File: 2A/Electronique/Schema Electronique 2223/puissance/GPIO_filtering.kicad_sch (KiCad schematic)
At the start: 4 parts, among them J201 Conn_01x02

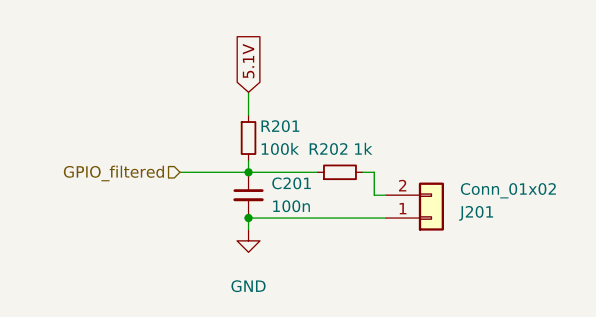
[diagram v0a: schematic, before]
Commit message: suppression diode et changement des feuille hiérarchique
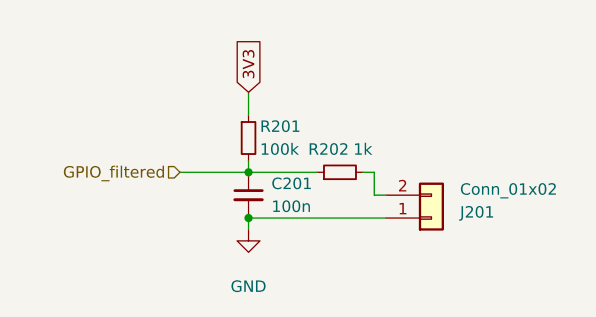
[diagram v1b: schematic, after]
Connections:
- net 5.1V renamed 3V3
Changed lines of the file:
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@@
     (stroke (width 0) (type default))
   )
-  (global_label "5.1V" (shape input) (at 124.46 73.66 90) (fields_autoplaced)
+  (global_label "3V3" (shape input) (at 124.46 73.66 90) (fields_autoplaced)
     (effects (font (size 1.27 1.27)) (justify left))
-    (property "Intersheetrefs" "${INTERSHEET_REFS}" (at 124.46 66.5624 90)
+    (property "Intersheetrefs" "${INTERSHEET_REFS}" (at 124.46 67.1672 90)
       (effects (font (size 1.27 1.27)) (justify left) hide)
     )

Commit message: update puissance
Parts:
- removed C201: 100n, Capacitor_SMD:C_0402_1005Metric, symbol Device:C_Small
- removed J201: Conn_01x02, symbol Connector_Generic:Conn_01x02
- removed R201: 100k, Resistor_SMD:R_0402_1005Metric, symbol Device:R_Small
- removed R202: 1k, Resistor_SMD:R_0402_1005Metric, symbol Device:R_Small
- added C2: 100n, Capacitor_SMD:C_0402_1005Metric, symbol Device:C_Small
- added J16: Conn_FDC, Connector_JST:JST_XH_B2B-XH-A_1x02_P2.50mm_Vertical, symbol Connector_Generic:Conn_01x02
- added R5: 100k, Resistor_SMD:R_0402_1005Metric, symbol Device:R_Small
- added R6: 1k, Resistor_SMD:R_0402_1005Metric, symbol Device:R_Small
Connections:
- net GND: now also C2.2, J16.1 (Pin_1)
- net GPIO_filtered: now also C2.1, R5.2, R6.1
- new net: J16.2 (Pin_2), R6.2
- new net PWR: R5.1
